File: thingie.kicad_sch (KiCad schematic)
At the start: 85 parts, among them J1 Conn_01x01_Male, J10 Conn_01x01_Male, J11 Conn_01x01_Male, J12 Conn_01x01_Male, J13 Conn_01x01_Male, J14 Conn_01x01_Male, J15 Conn_01x01_Male, J16 Conn_01x01_Male, J17 Conn_01x01_Male, J18 Conn_01x01_Male, J19 Conn_01x01_Male, J2 Conn_01x01_Male, J20 Conn_01x01_Male, J21 Conn_01x01_Male, J22 Conn_01x01_Male, J23 Conn_01x01_Male, J24 Conn_01x01_Male, J25 Conn_01x01_Male, J26 Conn_01x01_Male, J27 Conn_01x01_Male, J28 Conn_01x01_Male, J29 Conn_01x01_Male, J3 Conn_01x01_Male, J30 Conn_01x01_Male, J31 Conn_01x01_Male, J32 Conn_01x01_Male, J33 Conn_01x01_Male, J34 Conn_01x01_Male, J35 Conn_01x01_Male, J36 AudioJack4, J37 Conn_01x01_Male, J38 Conn_01x01_Male, J39 Conn_01x01_Male, J4 Conn_01x01_Male, J40 Conn_01x01_Male, J41 Conn_01x01_Male, J42 Conn_01x01_Male, J43 Conn_01x01_Male, J5 Conn_01x01_Male, J6 Conn_01x01_Male, J7 Conn_01x01_Male, J8 Conn_01x12, J9 Conn_01x01_Male, Q1 Q_NPN_BEC, Q2 Q_NMOS_DGS, SW1 SW_Push, SW13 SW_Push, SW14 SW_Push, U1 buttonarray, U2 SGTL5000XNAA3, U3 AP7313, U4 LTC1733, U5 DS2782, U6 TPS2116

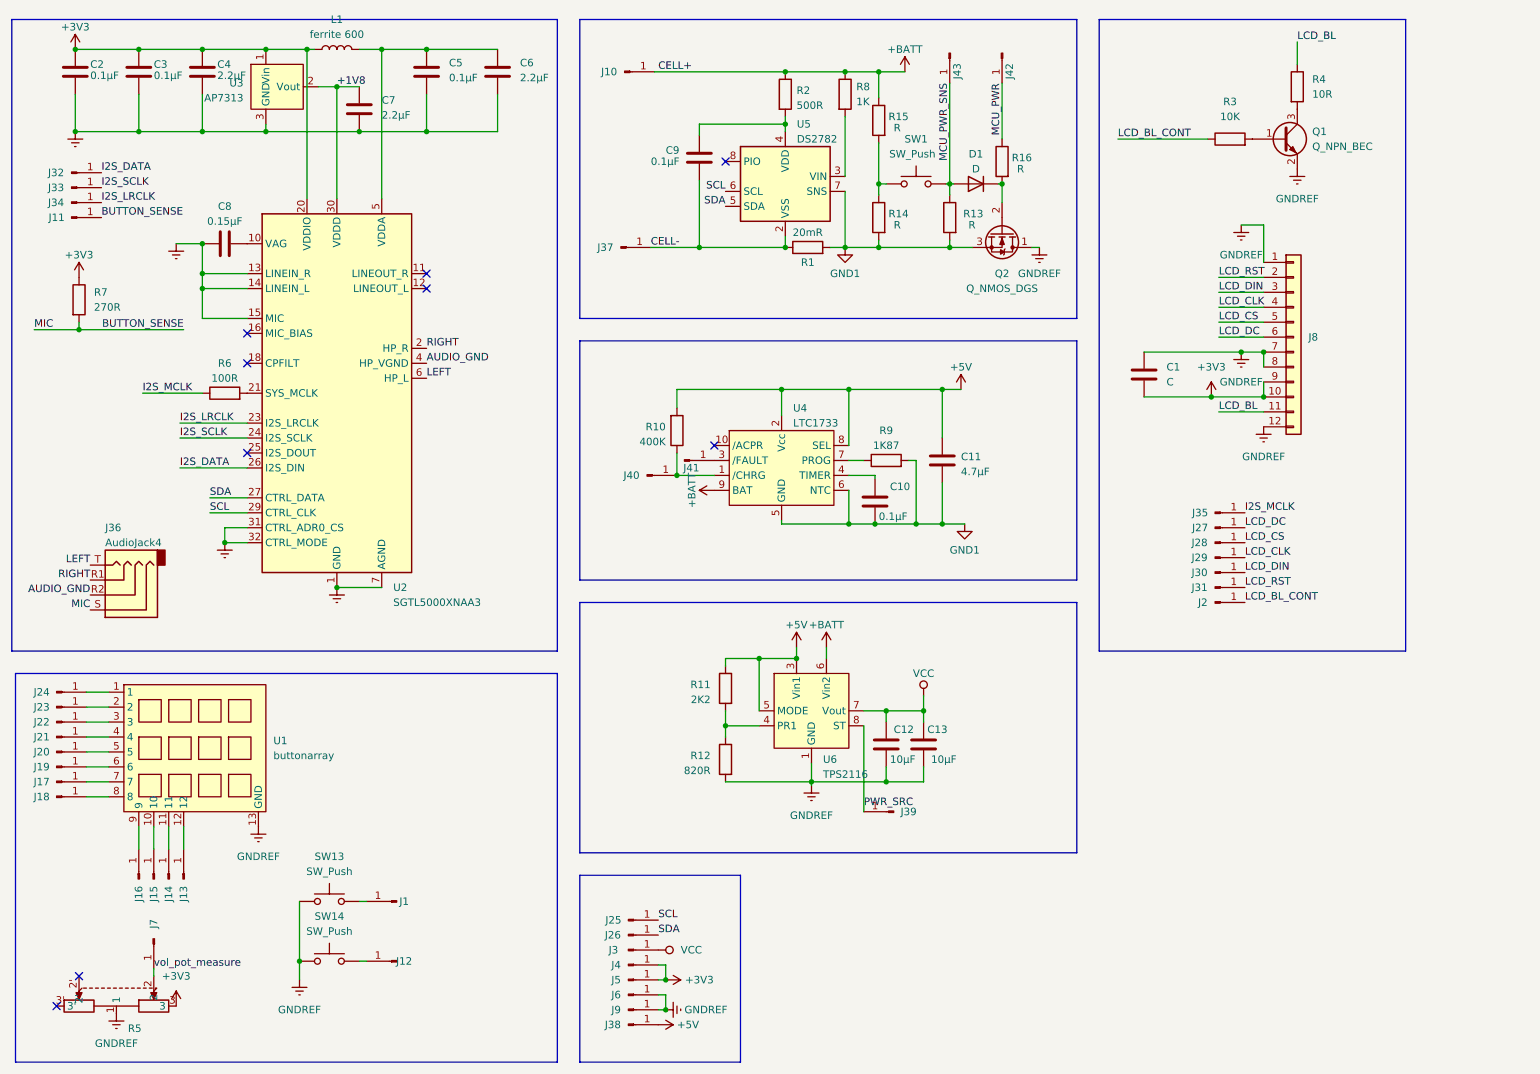
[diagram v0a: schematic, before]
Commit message: start modifying the schematic in preperation to add an RP2350
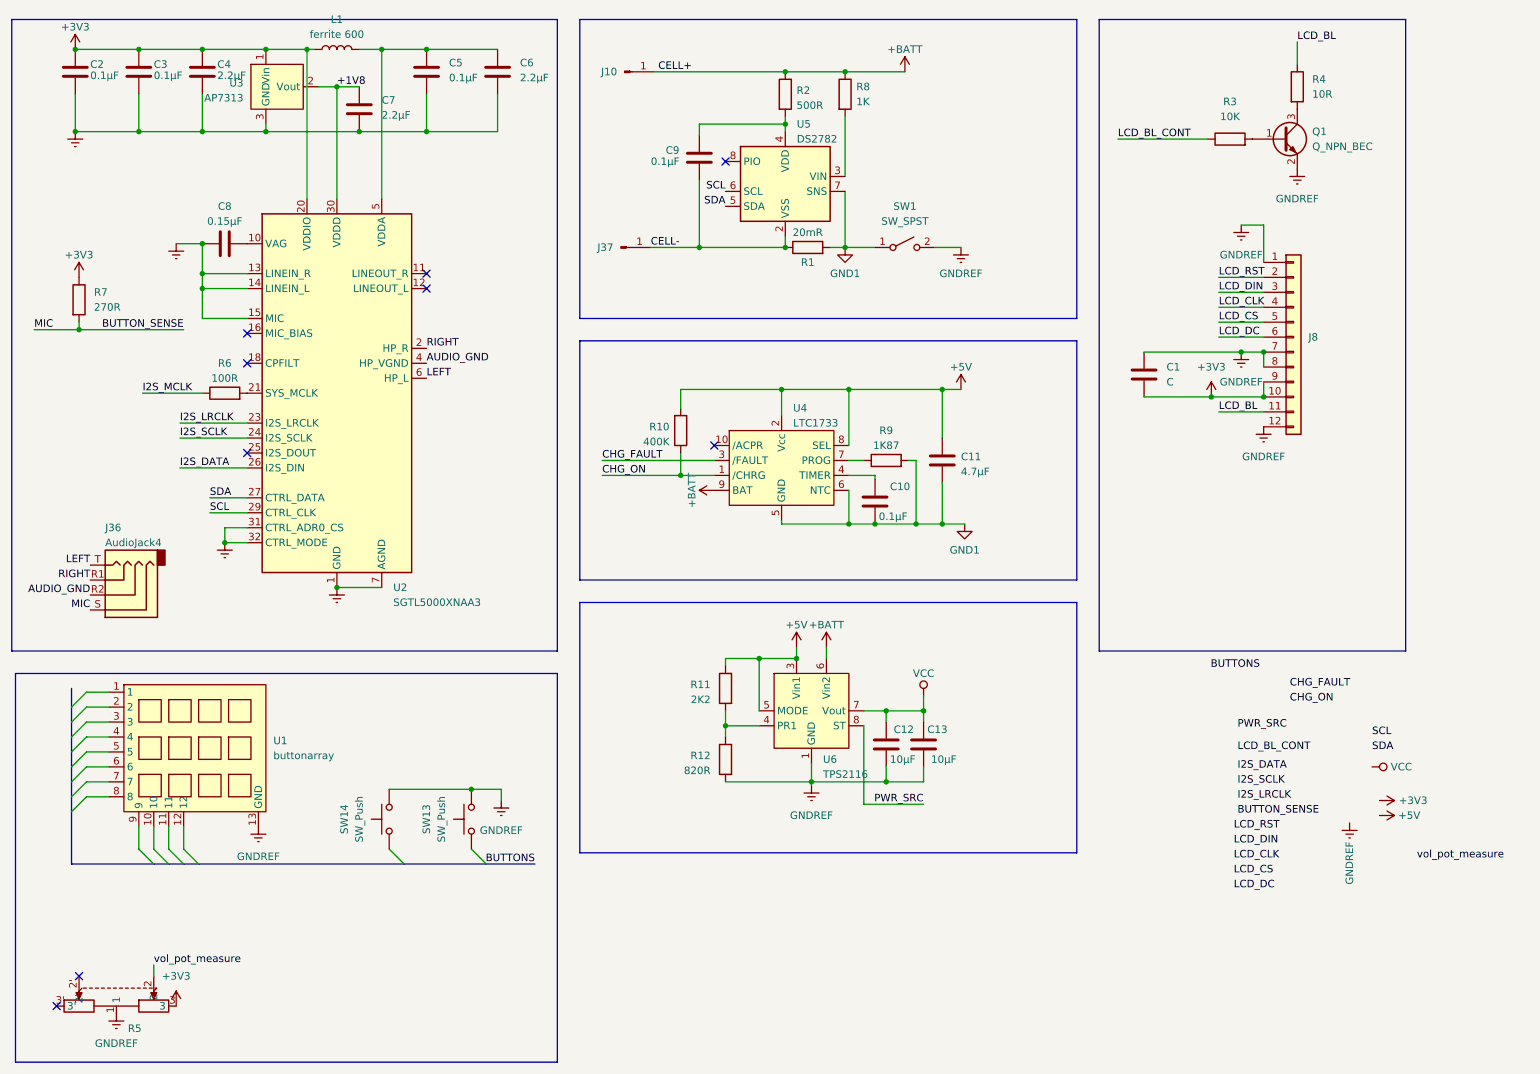
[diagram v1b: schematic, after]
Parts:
- removed D1: D, symbol Device:D
- removed J1, J11, J12, J13, J14, J15, J16, J17, J18, J19, J2, J20, J21, J22, J23, J24, J25, J26, J27, J28, J29, J3, J30, J31, J32, J33, J34, J35, J38, J39, J4, J40, J41, J42, J43, J5, J6, J7, J9: Conn_01x01_Male, custom_footprints:hole, symbol Connector:Conn_01x01_Male
- removed Q2: Q_NMOS_DGS, symbol Device:Q_NMOS_DGS
- removed R13, R14, R15, R16: R, symbol Device:R
- removed SW1: SW_Push, Button_Switch_THT:SW_PUSH_6mm_H5mm, symbol Switch:SW_Push
- added SW1: SW_SPST, symbol Switch:SW_SPST
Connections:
- net GND1: now also SW1.1 (A)
- net GNDREF: now also SW13.2, SW14.2, SW1.2 (B); no longer SW13.1, SW14.1
- net CHG_ON: now reaches R10.1, U4.1 (/CHRG)
- net CHG_FAULT: now reaches U4.3 (/FAULT)
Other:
- moved on the sheet: R10, SW13, SW14

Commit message: new µc schematic - it ain't all fitting on the PCB. Hmph.
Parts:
- added C14, C18, C32, C33: 10u, Capacitor_SMD:C_0805_2012Metric, symbol Device:C
- added C15, C16: 15p, Capacitor_SMD:C_0402_1005Metric, symbol Device:C
- added C17, C21, C24, C25, C26, C27, C28, C29, C30, C31: 100n, Capacitor_SMD:C_0402_1005Metric, symbol Device:C
- added C19, C20: 4.7u, Capacitor_SMD:C_0402_1005Metric_Pad0.74x0.62mm_HandSolder, symbol Device:C
- added C22, C23: 4.7u, Capacitor_SMD:C_0402_1005Metric, symbol Device:C
- added J2: Micro_SD_Card_Det, CM4IO:SDCARD_MOLEX_503398-1892, symbol Connector:Micro_SD_Card_Det
- added J3: USB_C_Receptacle_USB2.0_14P, Capacitor_SMD:C_0402_1005Metric_Pad0.74x0.62mm_HandSolder, symbol Connector:USB_C_Receptacle_USB2.0_14P
- added L2: 3.3u, RP2350_60QFN_minimal:L_pol_2016, symbol Device:L
- added R13, R15: DNF, Resistor_SMD:R_0402_1005Metric, symbol Device:R
- added R14: 0, Resistor_SMD:R_0402_1005Metric, symbol Device:R
- added R16, R17, R19: 1k, Resistor_SMD:R_0402_1005Metric, symbol Device:R
- added R18: 33, Resistor_SMD:R_0402_1005Metric, symbol Device:R
- added R20, R21: 27, Resistor_SMD:R_0402_1005Metric, symbol Device:R
- added R22: 12K 1%, Resistor_SMD:R_0402_1005Metric, symbol Device:R
- added SW2, SW3: SW_Push, Button_Switch_SMD:SW_Push_1P1T_NO_Vertical_Wuerth_434133025816, symbol Switch:SW_Push
- added U10: RT9742GGJ5, Package_TO_SOT_SMD:SOT-23-5, symbol CM4IO:RT9742GGJ5
- added U7: W25Q128JVS, Package_SO:SOIC-8_5.23x5.23mm_P1.27mm, symbol Memory_Flash:W25Q128JVS
- added U8: NCP1117-3.3_SOT223, Package_TO_SOT_SMD:SOT-223-3_TabPin2, symbol Regulator_Linear:NCP1117-3.3_SOT223
- added U9: RP2350_60QFN, RP2350_60QFN_minimal:RP2350-QFN-60-1EP_7x7_P0.4mm_EP3.4x3.4mm_ThermalVias, symbol MCU_RaspberryPi_RP2350:RP2350_60QFN
- added Y1: ABM8-272-T3, Crystal:Crystal_SMD_3225-4Pin_3.2x2.5mm, symbol Device:Crystal_GND24
- SW1: footprint (none) -> Button_Switch_SMD:SW_Push_1P1T-SH_NO_CK_KMR2xxG
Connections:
- net +3V3: now also C17.1, C18.1, C19.1, C25.1, C26.1, C27.1, C28.1, C29.1, C30.1, C31.1, C32.1, R15.1, R18.1, U7.8 (VCC), U8.2 (VO), U9.1 (IOVDD), U9.11 (IOVDD), U9.20 (IOVDD), U9.30 (IOVDD), U9.38 (IOVDD), U9.44 (ADC_AVDD), U9.45 (IOVDD), U9.49 (VREG_VIN), U9.53 (USB_OTP_VDD), U9.54 (QSPI_IOVDD)
- net GNDREF: now also C14.2, C15.2, C16.2, C17.2, C18.2, C19.2, C20.2, C21.2, C22.2, C23.2, C24.2, C25.2, C26.2, C27.2, C28.2, C29.2, C30.2, C31.2, C32.2, C33.2, J2.11 (SHIELD), J2.6 (VSS), J3.A1 (GND), J3.A12 (GND), J3.B1 (GND), J3.B12 (GND), J3.S1 (SHIELD), R17.2, SW2.1, U10.2 (GND), U8.1 (GND), U9.47 (VREG_PGND), U9.61 (GND)
- new net: R17.1, SW3.1
- new net: R20.2, U9.52 (USB_DP)
- new net: C16.1, R16.2, Y1.3
- new net: R21.2, U9.51 (USB_DM)
- new net +1V1: C20.1, C21.1, C23.1, C24.1, L2.1, U9.23 (DVDD), U9.39 (DVDD), U9.50 (VREG_FB), U9.6 (DVDD)
- new net +3.3v: R22.1, U10.5 (IN)
- new net FLASH_SS: R13.2, R14.2, R15.2, U7.1 (~{CS})
- new net GND: Y1.2, Y1.4
- new net GPIO0: R13.1
- new net QSPI_SCLK: U7.6 (CLK), U9.56 (QSPI_SCLK)
- new net QSPI_SD0: U7.5 (DI(IO0)), U9.57 (QSPI_SD0)
- new net QSPI_SD1: U7.2 (DO(IO1)), U9.59 (QSPI_SD1)
- new net QSPI_SD2: U7.3 (IO2), U9.58 (QSPI_SD2)
- new net QSPI_SD3: U7.7 (IO3), U9.55 (QSPI_SD3)
- new net QSPI_SS: R14.1, R19.1, U9.60 (QSPI_SS)
- new net RUN: SW3.2, U9.26 (RUN)
- new net SD_CLK: J2.5 (CLK)
- new net SD_CMD: J2.3 (CMD)
- new net SD_DAT0: J2.7 (DAT0)
- new net SD_DAT1: J2.8 (DAT1)
- new net SD_DAT2: J2.1 (DAT2)
- new net SD_DAT3: J2.2 (DAT3/CD)
- new net SD_PWR: C33.1, J2.4 (VDD), U10.1 (OUT)
- new net SD_PWR_ON: R22.2, U10.4 (EN)
- new net SWCLK: U9.24 (SWCLK)
- new net SWD: U9.25 (SWD)
- new net USB_D+: J3.A6 (D+), J3.B6 (D+), R20.1
- new net USB_D-: J3.A7 (D-), J3.B7 (D-), R21.1
- new net VBUS: C14.1, J3.A4 (VBUS), J3.A9 (VBUS), J3.B4 (VBUS), J3.B9 (VBUS), U8.3 (VI)
- new net VREG_AVDD: C22.1, R18.2, U9.46 (VREG_AVDD)
- new net VREG_LX: L2.2, U9.48 (VREG_LX)
- new net XIN: C15.1, U9.21 (XIN), Y1.1
- new net XOUT: R16.1, U9.22 (XOUT)
- new net ~{USB_BOOT}: R19.2, SW2.2
- no-connect marks 9 -> 14
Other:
- note added: "12MHz Crystal"
- note added: "Flash"
- note added: "Make sure R7 and R8 are close to RP2350"
- note added: "Power"
- moved on the sheet: C2, C3, C4
